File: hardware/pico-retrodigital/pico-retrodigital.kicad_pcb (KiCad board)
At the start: 2 copper layers, 50 x 38 mm, 70 parts, among them J1 Conn_02x05_Top_Bottom, J3 Conn_01x14, J4 Conn_01x02_Pin, J5 USB_C_Plug_USB2.0, U1 SN74LVC1G17DBVR, U2 SN74LVC1G17DBVR, U3 RP2354B, U4 SN74LVC245APW, U5 SN74LVC245APW, U6 SN74LVC245APW, U8 ME6217C33M5G, Y1 ABM8-272-T3

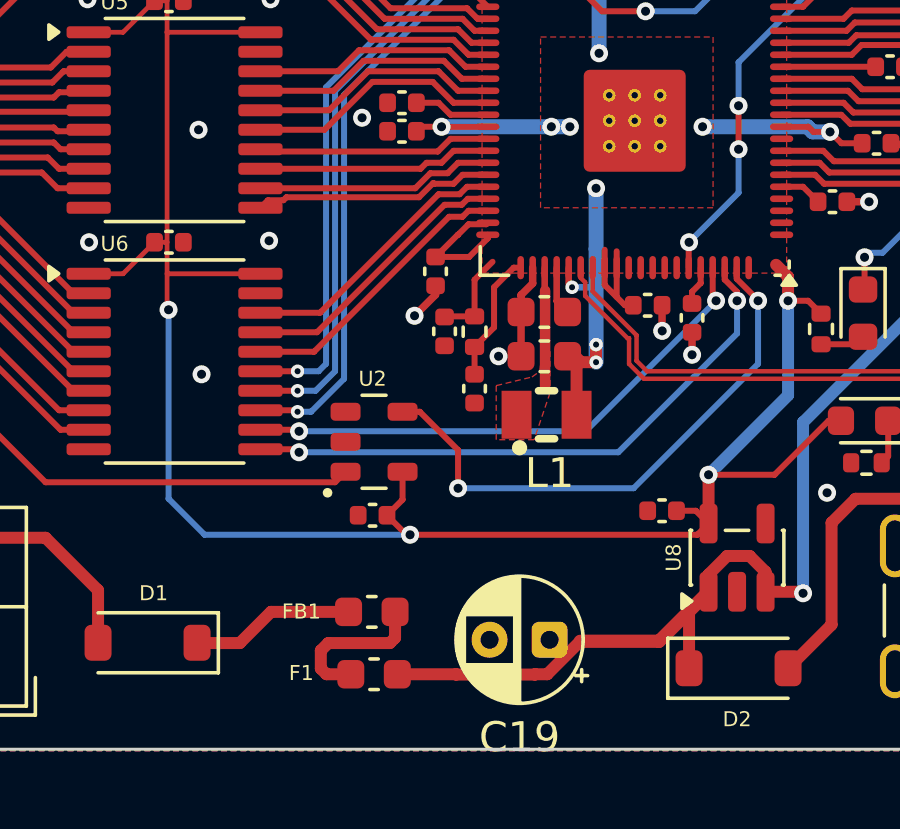
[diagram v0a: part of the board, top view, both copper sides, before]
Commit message: Add breakout board
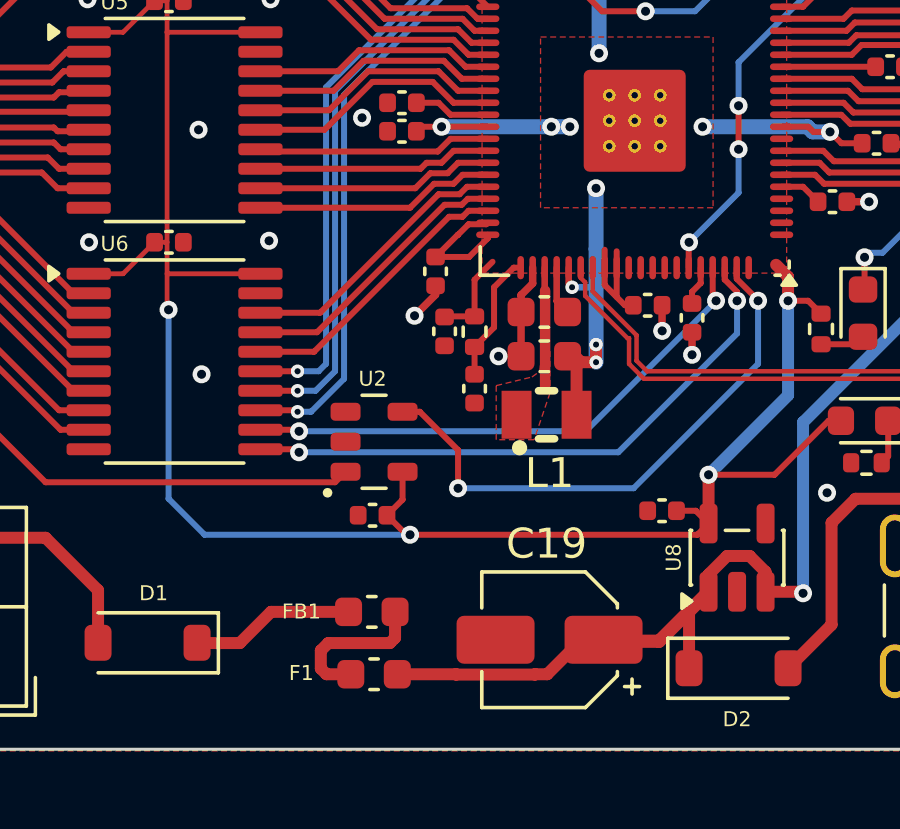
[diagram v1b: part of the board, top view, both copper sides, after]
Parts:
- C19: footprint Capacitor_THT:CP_Radial_D4.0mm_P2.00mm -> Capacitor_SMD:CP_Elec_4x3
